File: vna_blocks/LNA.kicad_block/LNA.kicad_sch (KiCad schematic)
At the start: 12 parts, among them IC5 LVA-273PN+

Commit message: new design blocks, footprints
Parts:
- removed C66, C77, C78, C79, C80, C81, C82: 100n, Capacitor_SMD:C_0402_1005Metric, symbol Device:C_Small
- removed C83: P21BNL300M5S, Capacitor_SMD:C_0201_0603Metric, symbol Device:C_Small
- removed C84: 10n, Capacitor_SMD:C_0402_1005Metric, symbol Device:C_Small
- removed C85: 1u, Capacitor_SMD:C_0402_1005Metric, symbol Device:C_Small
- removed L4: BCR272JLC, symbol Device:L_Small
- added C63, C64, C65, C68, C69, C70, C73: 100n, Capacitor_SMD:C_0402_1005Metric, symbol Device:C_Small
- added C74: P21BNL300M5S, Capacitor_SMD:C_0201_0603Metric, symbol Device:C_Small
- added C75: 10n, Capacitor_SMD:C_0402_1005Metric, symbol Device:C_Small
- added C76: 1u, Capacitor_SMD:C_0402_1005Metric, symbol Device:C_Small
- added L3: BCR272JLC, VNA_fp:BCR-272, symbol Device:L_Small
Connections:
- net GNDA: now also C63.1, C64.1, C65.2, C68.2, C69.2, C70.2, C73.2, C75.2, C76.2; no longer IC5.23 (GND_4), IC5.25 (GND_5)
- net at IC5.6 (CG1): now also C73.1
- net at IC5.18 (CG4): now also C65.1
- net at IC5.5 (CG2): now also C70.1
- net at IC5.3 (VB): now also C69.1
- net at IC5.1 (VC): now also C64.2
- net at IC5.17 (CG3): now also C68.1
- net at IC5.10 (RF-OUT_&_VCC): now also C74.1, L3.1
- net at IC5.20 (CG5): now also C63.2
- new net: C75.1, C76.1, L3.2

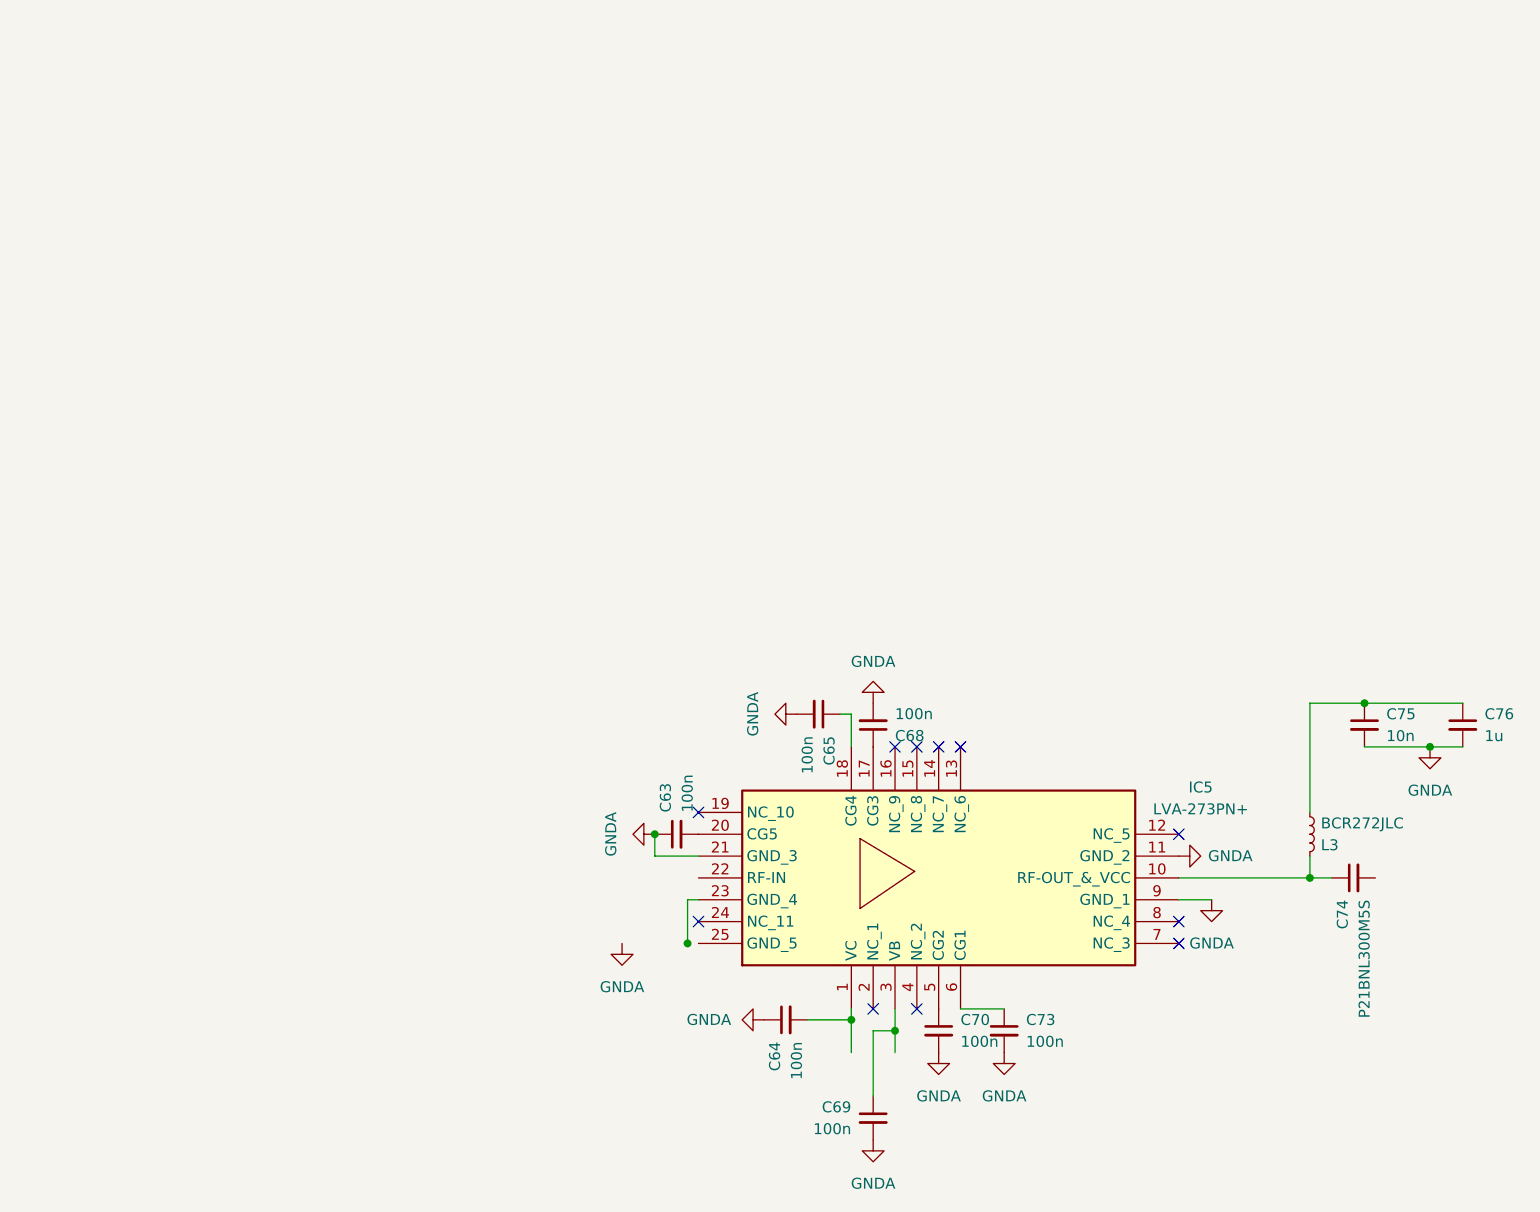
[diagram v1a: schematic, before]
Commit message: added BTM-0026 symbol and footprint
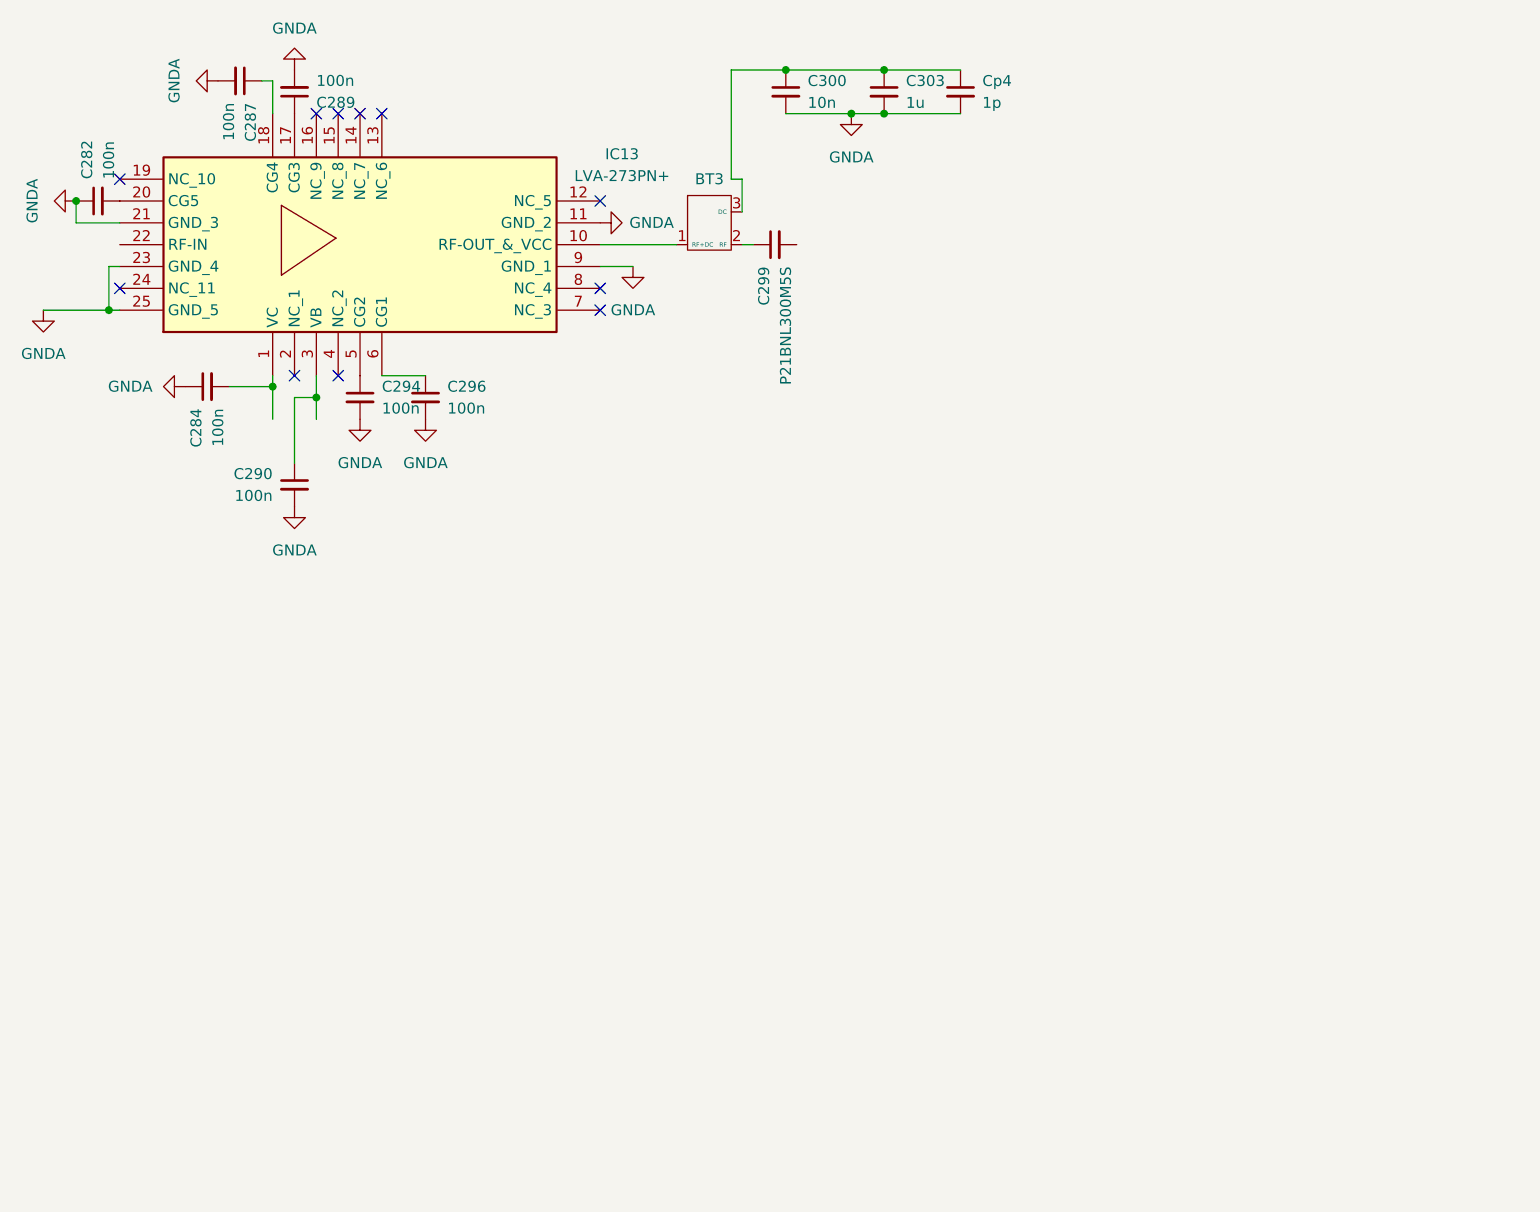
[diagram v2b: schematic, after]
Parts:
- removed C63, C64, C65, C68, C69, C70, C73: 100n, Capacitor_SMD:C_0402_1005Metric, symbol Device:C_Small
- removed C74: P21BNL300M5S, Capacitor_SMD:C_0201_0603Metric, symbol Device:C_Small
- removed C75: 10n, Capacitor_SMD:C_0402_1005Metric, symbol Device:C_Small
- removed C76: 1u, Capacitor_SMD:C_0402_1005Metric, symbol Device:C_Small
- removed IC5: LVA-273PN+, VNA_fp:DG1847_MNC-L, symbol VNA_sym:LVA-273PN+
- removed L3: BCR272JLC, VNA_fp:BCR-272, symbol Device:L_Small
- added BT3: (no value), symbol VNA_sym:BTM0026
- added C282, C284, C287, C289, C290, C294, C296: 100n, Capacitor_SMD:C_0402_1005Metric, symbol Device:C_Small
- added C299: P21BNL300M5S, VNA_fp:P21BN, symbol Device:C_Small
- added C300: 10n, Capacitor_SMD:C_0402_1005Metric, symbol Device:C_Small
- added C303: 1u, Capacitor_SMD:C_0402_1005Metric, symbol Device:C_Small
- added Cp4: 1p, Capacitor_SMD:C_0402_1005Metric, symbol Device:C_Small
- added IC13: LVA-273PN+, VNA_fp:DG1847_MNC-L, symbol VNA_sym:LVA-273PN+
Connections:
- net GNDA: now also C282.1, C284.1, C287.2, C289.2, C290.2, C294.2, C296.2, C300.2, C303.2, Cp4.2, IC13.11 (GND_2), IC13.21 (GND_3), IC13.23 (GND_4), IC13.25 (GND_5), IC13.9 (GND_1)
- new net: BT3.1 (RF+DC), IC13.10 (RF-OUT_&_VCC)
- new net: BT3.2 (RF), C299.1
- new net: BT3.3 (DC), C300.1, C303.1, Cp4.1
- new net: C294.1, IC13.5 (CG2)
- new net: C287.1, IC13.18 (CG4)
- new net: C290.1, IC13.3 (VB)
- new net: C284.2, IC13.1 (VC)
- new net: C289.1, IC13.17 (CG3)
- new net: C282.2, IC13.20 (CG5)
- new net: C296.1, IC13.6 (CG1)

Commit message: fixed IC courtyard issues
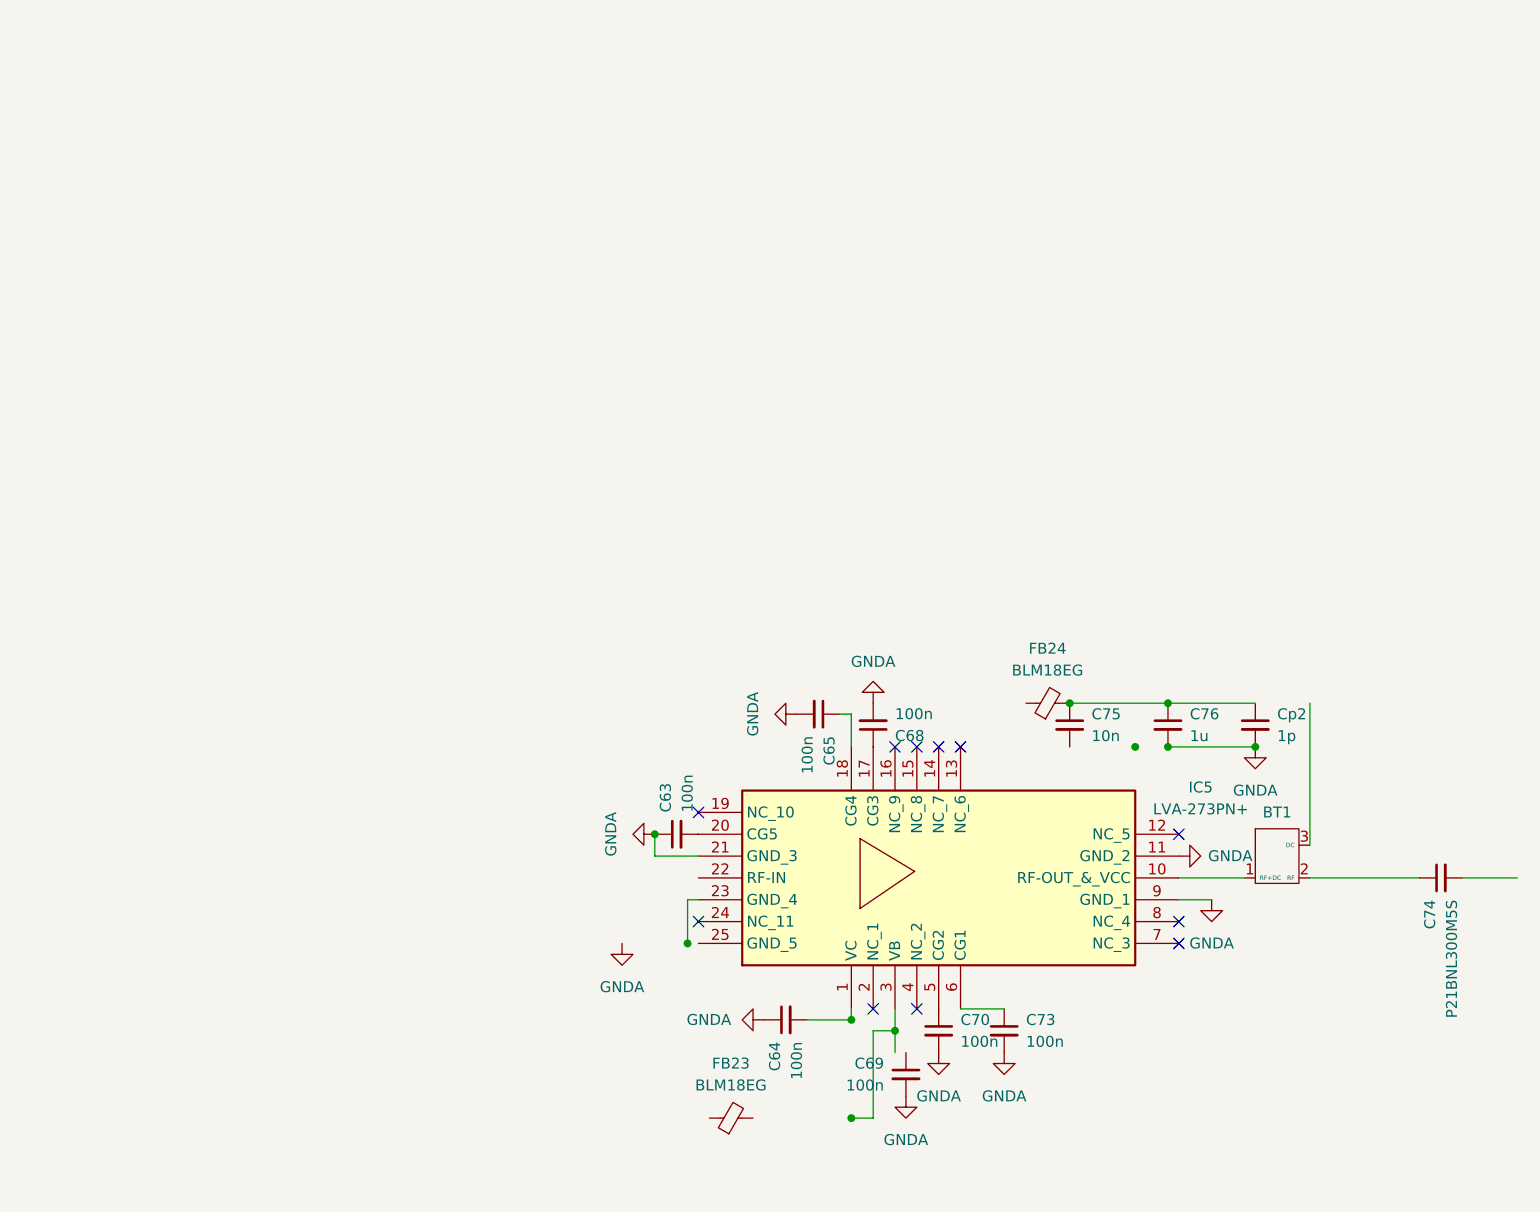
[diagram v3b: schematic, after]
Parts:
- removed BT3: (no value), symbol VNA_sym:BTM0026
- removed C282, C284, C287, C289, C290, C294, C296: 100n, Capacitor_SMD:C_0402_1005Metric, symbol Device:C_Small
- removed C299: P21BNL300M5S, VNA_fp:P21BN, symbol Device:C_Small
- removed C300: 10n, Capacitor_SMD:C_0402_1005Metric, symbol Device:C_Small
- removed C303: 1u, Capacitor_SMD:C_0402_1005Metric, symbol Device:C_Small
- removed Cp4: 1p, Capacitor_SMD:C_0402_1005Metric, symbol Device:C_Small
- removed IC13: LVA-273PN+, VNA_fp:DG1847_MNC-L, symbol VNA_sym:LVA-273PN+
- added BT1: (no value), VNA_fp:BTM-0026, symbol VNA_sym:BTM0026
- added C63, C64, C65, C68, C69, C70, C73: 100n, Capacitor_SMD:C_0402_1005Metric, symbol Device:C_Small
- added C74: P21BNL300M5S, VNA_fp:P21BN, symbol Device:C_Small
- added C75: 10n, Capacitor_SMD:C_0402_1005Metric, symbol Device:C_Small
- added C76: 1u, Capacitor_SMD:C_0402_1005Metric, symbol Device:C_Small
- added Cp2: 1p, Capacitor_SMD:C_0402_1005Metric, symbol Device:C_Small
- added FB23, FB24: BLM18EG, Inductor_SMD:L_0603_1608Metric, symbol Device:FerriteBead_Small
- added IC5: LVA-273PN+, VNA_fp:DG1847_MNC-L, symbol VNA_sym:LVA-273PN+
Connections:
- net GNDA: now also C63.1, C64.1, C65.2, C68.2, C69.2, C70.2, C73.2, C76.2, Cp2.2, IC5.11 (GND_2), IC5.21 (GND_3), IC5.9 (GND_1)
- new net: C75.1, C76.1, Cp2.1, FB24.2
- new net: BT1.1 (RF+DC), IC5.10 (RF-OUT_&_VCC)
- new net: BT1.2 (RF), C74.1
- new net: C68.1, IC5.17 (CG3)
- new net: C63.2, IC5.20 (CG5)
- new net: C64.2, IC5.1 (VC)
- new net: C65.1, IC5.18 (CG4)
- new net: C70.1, IC5.5 (CG2)
- new net: C73.1, IC5.6 (CG1)
